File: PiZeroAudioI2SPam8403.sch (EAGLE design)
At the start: 60 parts, among them CON1 RPI-ZERO, J1 GROVE, J2 2X2HEADER, J3 JST, J4 AMP FCI 10103594-0001LF, J5 2X1-LOCKING, J6 GROVE, J7 4X1-LOCKING, Q1 DMG2305UX, U1 TXB0104PWR, U2 LSM6DS33, U3 PCM5101A, U4 MCP73831, U5 DMMT5401, U6 TXS0102, U7 PAM8403, U8 PAM2401

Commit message: Made Values consistent with Upper case K
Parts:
- R14: value 100k -> 100K
- R7: value 1k -> 1K
- R8: value 2.0k -> 2K
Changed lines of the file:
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@@
 <part name="C13" library="rcl" library_urn="urn:adsk.eagle:library:334" deviceset="C-EU" device="C0603" package3d_urn="urn:adsk.eagle:package:23616/2" value="4.7uF"/>
 <part name="D1" library="SparkFun-LED" deviceset="LED-BLUE" device="0603" value="BLUE"/>
-<part name="R7" library="adafruit" deviceset="R-US_" device="R0603" value="1k"/>
-<part name="R8" library="adafruit" deviceset="R-US_" device="R0603" value="2.0k"/>
+<part name="R7" library="adafruit" deviceset="R-US_" device="R0603" value="1K"/>
+<part name="R8" library="adafruit" deviceset="R-US_" device="R0603" value="2K"/>
 <part name="U4" library="SparkFun-IC-Power" deviceset="MCP73831" device=""/>
 <part name="R12" library="adafruit" deviceset="R-US_" device="R0603" value="750K"/>
-<part name="R14" library="adafruit" deviceset="R-US_" device="R0603" value="100k"/>
+<part name="R14" library="adafruit" deviceset="R-US_" device="R0603" value="100K"/>
 <part name="R15" library="adafruit" deviceset="R-US_" device="R0603" value="100K"/>
 <part name="U8" library="SparkFun-IC-Power" deviceset="PAM2401" device="" value="PAM2401"/>

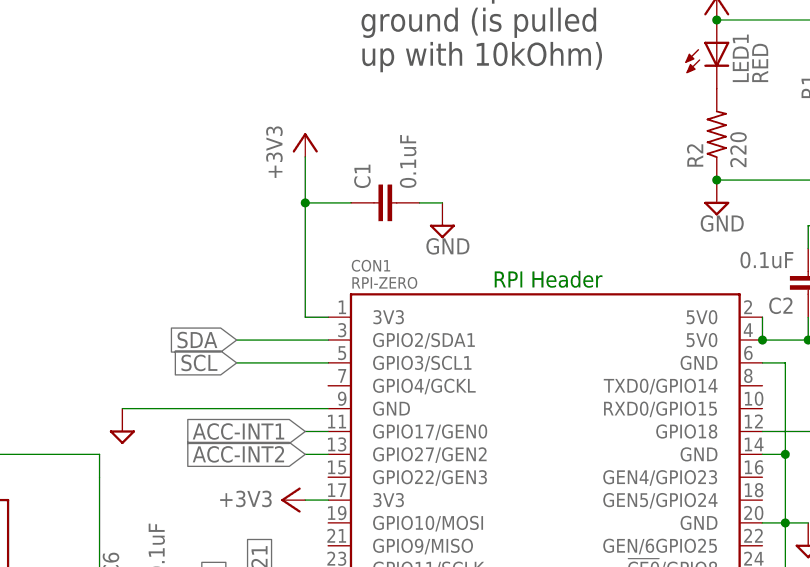
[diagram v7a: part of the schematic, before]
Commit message: Changed the name of RPI Header
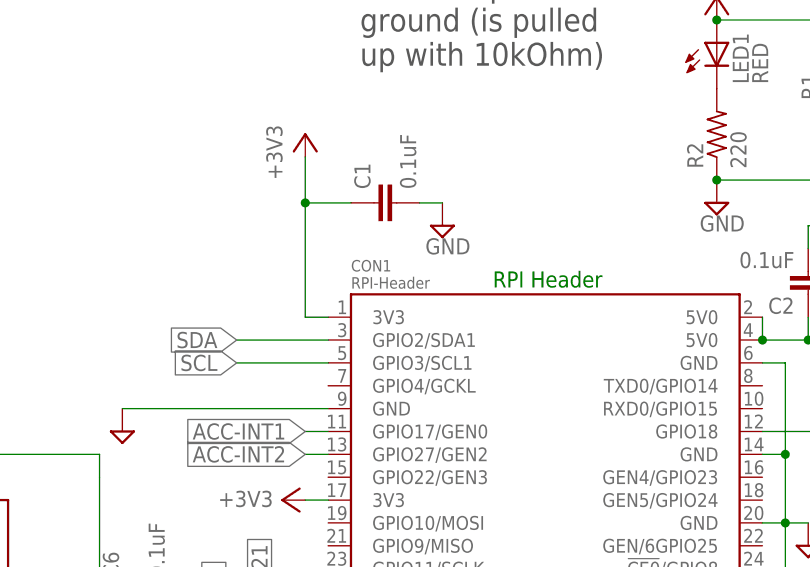
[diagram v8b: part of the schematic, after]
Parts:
- CON1: value RPI-ZERO -> RPI-Header
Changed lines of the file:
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@@
 </classes>
 <parts>
-<part name="CON1" library="RPI-Zero" deviceset="RPI-ZERO" device=""/>
+<part name="CON1" library="RPI-Zero" deviceset="RPI-ZERO" device="" value="RPI-Header"/>
 <part name="P+3" library="supply1" library_urn="urn:adsk.eagle:library:371" deviceset="+5V" device=""/>
 <part name="+3V33" library="supply1" library_urn="urn:adsk.eagle:library:371" deviceset="+3V3" device=""/>
